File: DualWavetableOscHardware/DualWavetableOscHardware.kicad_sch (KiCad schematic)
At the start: 102 parts, among them J103 SWD Header, J106 CV1, J106 CV2, J106 MOD1, J106 MOD2, J106 OUT1, J106 OUT2, J109 Micro_SD_Card, J109 POWER, SW101 BOOT, SW101 RST, SW219 CH, SW219 MODE, SW221 ENC1, SW221 ENC2, U101 STM32F410CBTx, U106 AMS1117, U402 TL072, U403 PCM5100A, Y101 16MHz

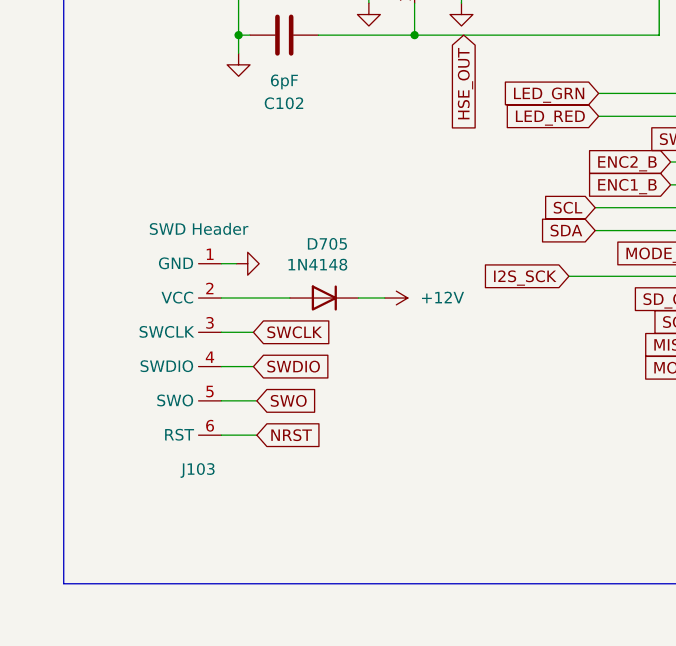
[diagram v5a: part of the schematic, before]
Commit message: new stackup/routing
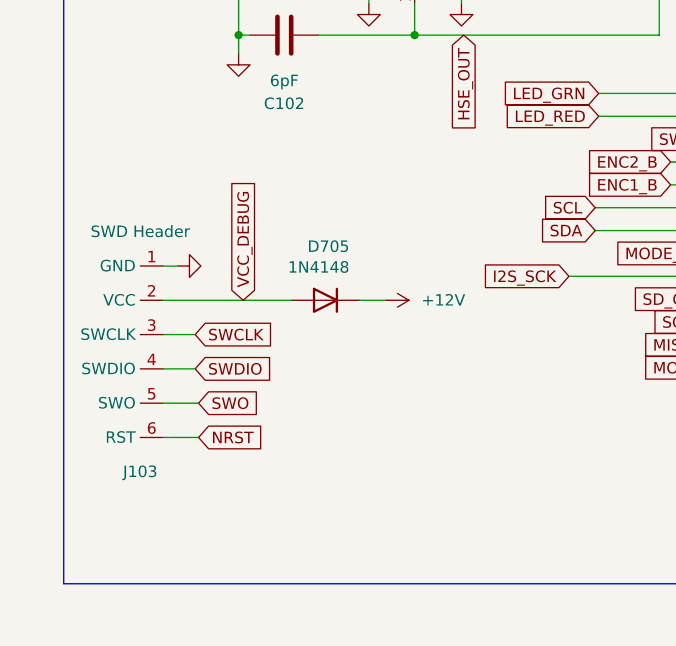
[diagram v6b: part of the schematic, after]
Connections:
- net VCC_DEBUG: now reaches D705.2 (A), J103.2 (VCC)
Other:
- moved on the sheet: J103
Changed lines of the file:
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@@
     (stroke (width 0) (type default))
   )
-  (wire (pts (xy 53.467 116.205) (xy 56.388 116.205))
+  (wire (pts (xy 53.594 116.459) (xy 56.515 116.459))
     (stroke (width 0) (type default))
   )
@@
     (stroke (width 0) (type default))
   )
-  (wire (pts (xy 38.227 116.205) (xy 45.847 116.205))
+  (wire (pts (xy 31.75 116.459) (xy 45.974 116.459))
     (stroke (width 0) (type default))
   )
@@
     (stroke (width 0) (type default))
   )
-  (wire (pts (xy 38.227 123.825) (xy 41.783 123.825))
+  (wire (pts (xy 31.75 124.079) (xy 35.306 124.079))
     (stroke (width 0) (type default))
   )
@@
     (stroke (width 0) (type default))
   )
-  (wire (pts (xy 38.227 120.015) (xy 41.783 120.015))
+  (wire (pts (xy 31.75 120.269) (xy 35.306 120.269))
     (stroke (width 0) (type default))
   )
@@
     (stroke (width 0) (type default))
   )
-  (wire (pts (xy 38.227 112.395) (xy 39.878 112.395))
+  (wire (pts (xy 31.75 112.649) (xy 33.401 112.649))
     (stroke (width 0) (type default))
   )
@@
     (stroke (width 0) (type default))
   )
-  (wire (pts (xy 38.227 131.445) (xy 42.164 131.445))
+  (wire (pts (xy 31.75 131.699) (xy 35.687 131.699))
     (stroke (width 0) (type default))
   )
@@
     (stroke (width 0) (type default))
   )
-  (wire (pts (xy 38.227 127.635) (xy 42.164 127.635))
+  (wire (pts (xy 31.75 127.889) (xy 35.687 127.889))
     (stroke (width 0) (type default))
   )
@@
     )
   )
-  (global_label "SWCLK" (shape input) (at 41.783 120.015 0) (fields_autoplaced)
+  (global_label "SWCLK" (shape input) (at 35.306 120.269 0) (fields_autoplaced)
     (effects (font (size 1.27 1.27)) (justify left))
-    (property "Intersheetrefs" "${INTERSHEET_REFS}" (at 50.9972 120.015 0)
+    (property "Intersheetrefs" "${INTERSHEET_REFS}" (at 44.5202 120.269 0)
       (effects (font (size 1.27 1.27)) (justify left) hide)
     )
@@
     )
   )
+  (global_label "VCC_DEBUG" (shape input) (at 40.64 116.459 90) (fields_autoplaced)
+    (effects (font (size 1.27 1.27)) (justify left))
+    (property "Intersheetrefs" "${INTERSHEET_REFS}" (at 40.64 102.5881 90)
+      (effects (font (size 1.27 1.27)) (justify left) hide)
+    )
+  )
   (global_label "SCL" (shape input) (at 79.756 106.172 180) (fields_autoplaced)
     (effects (font (size 1.27 1.27)) (justify right))
@@
     )
   )
-  (global_label "SWDIO" (shape input) (at 41.783 123.825 0) (fields_autoplaced)
+  (global_label "SWDIO" (shape input) (at 35.306 124.079 0) (fields_autoplaced)
     (effects (font (size 1.27 1.27)) (justify left))
-    (property "Intersheetrefs" "${INTERSHEET_REFS}" (at 50.6344 123.825 0)
+    (property "Intersheetrefs" "${INTERSHEET_REFS}" (at 44.1574 124.079 0)
       (effects (font (size 1.27 1.27)) (justify left) hide)
     )
@@
     )
   )
-  (global_label "NRST" (shape input) (at 42.164 131.445 0) (fields_autoplaced)
+  (global_label "NRST" (shape input) (at 35.687 131.699 0) (fields_autoplaced)
     (effects (font (size 1.27 1.27)) (justify left))
-    (property "Intersheetrefs" "${INTERSHEET_REFS}" (at 49.9268 131.445 0)
+    (property "Intersheetrefs" "${INTERSHEET_REFS}" (at 43.4498 131.699 0)
       (effects (font (size 1.27 1.27)) (justify left) hide)
     )
   )
-  (global_label "SWO" (shape input) (at 42.164 127.635 0) (fields_autoplaced)
+  (global_label "SWO" (shape input) (at 35.687 127.889 0) (fields_autoplaced)
     (effects (font (size 1.27 1.27)) (justify left))
-    (property "Intersheetrefs" "${INTERSHEET_REFS}" (at 49.1406 127.635 0)
+    (property "Intersheetrefs" "${INTERSHEET_REFS}" (at 42.6636 127.889 0)
       (effects (font (size 1.27 1.27)) (justify left) hide)
     )
@@
     )
   )
-  (symbol (lib_id "Diode:1N4148") (at 49.657 116.205 0) (mirror y) (unit 1)
+  (symbol (lib_id "Diode:1N4148") (at 49.784 116.459 0) (mirror y) (unit 1)
     (in_bom yes) (on_board yes) (dnp no)
-    (property "Reference" "D705" (at 52.324 110.236 0)
+    (property "Reference" "D705" (at 52.451 110.49 0)
       (effects (font (size 1.27 1.27)) (justify left))
     )
-    (property "Value" "1N4148" (at 52.324 112.5474 0)
+    (property "Value" "1N4148" (at 52.451 112.8014 0)
       (effects (font (size 1.27 1.27)) (justify left))
     )
-    (property "Footprint" "Diode_SMD:D_SOD-123" (at 49.657 116.205 0)
+    (property "Footprint" "Diode_SMD:D_SOD-123" (at 49.784 116.459 0)
       (effects (font (size 1.27 1.27)) hide)
     )
-    (property "Datasheet" "https://assets.nexperia.com/documents/data-sheet/1N4148_1N4448.pdf" (at 49.657 116.205 0)
+    (property "Datasheet" "https://assets.nexperia.com/documents/data-sheet/1N4148_1N4448.pdf" (at 49.784 116.459 0)
       (effects (font (size 1.27 1.27)) hide)
     )
-    (property "Sim.Device" "D" (at 49.657 116.205 0)
+    (property "Sim.Device" "D" (at 49.784 116.459 0)
       (effects (font (size 1.27 1.27)) hide)
     )
-    (property "Sim.Pins" "1=K 2=A" (at 49.657 116.205 0)
+    (property "Sim.Pins" "1=K 2=A" (at 49.784 116.459 0)
       (effects (font (size 1.27 1.27)) hide)
     )
@@
     )
   )
-  (symbol (lib_id "power:GND") (at 39.878 112.395 90) (unit 1)
+  (symbol (lib_id "power:GND") (at 33.401 112.649 90) (unit 1)
     (in_bom yes) (on_board yes) (dnp no) (fields_autoplaced)
-    (property "Reference" "#PWR0108" (at 46.228 112.395 0)
+    (property "Reference" "#PWR0108" (at 39.751 112.649 0)
       (effects (font (size 1.27 1.27)) hide)
     )
-    (property "Value" "GND" (at 43.688 112.395 0)
+    (property "Value" "GND" (at 37.211 112.649 0)
       (effects (font (size 1.27 1.27)) hide)
     )
-    (property "Footprint" "" (at 39.878 112.395 0)
+    (property "Footprint" "" (at 33.401 112.649 0)
       (effects (font (size 1.27 1.27)) hide)
     )
-    (property "Datasheet" "" (at 39.878 112.395 0)
+    (property "Datasheet" "" (at 33.401 112.649 0)
       (effects (font (size 1.27 1.27)) hide)
     )
@@
     )
   )
-  (symbol (lib_id "power:+12V") (at 56.388 116.205 270) (unit 1)
+  (symbol (lib_id "power:+12V") (at 56.515 116.459 270) (unit 1)
     (in_bom yes) (on_board yes) (dnp no) (fields_autoplaced)
-    (property "Reference" "#PWR0107" (at 52.578 116.205 0)
+    (property "Reference" "#PWR0107" (at 52.705 116.459 0)
       (effects (font (size 1.27 1.27)) hide)
     )
-    (property "Value" "+12V" (at 60.325 116.205 90)
+    (property "Value" "+12V" (at 60.452 116.459 90)
       (effects (font (size 1.27 1.27)) (justify left))
     )
-    (property "Footprint" "" (at 56.388 116.205 0)
+    (property "Footprint" "" (at 56.515 116.459 0)
       (effects (font (size 1.27 1.27)) hide)
     )
-    (property "Datasheet" "" (at 56.388 116.205 0)
+    (property "Datasheet" "" (at 56.515 116.459 0)
       (effects (font (size 1.27 1.27)) hide)
     )
@@
     )
   )
-  (symbol (lib_id "Connector:ST_SWDHeader_3Wire") (at 35.687 135.255 0) (unit 1)
+  (symbol (lib_id "Connector:ST_SWDHeader_3Wire") (at 29.21 135.509 0) (unit 1)
     (in_bom yes) (on_board yes) (dnp no) (fields_autoplaced)
-    (property "Reference" "J103" (at 35.687 135.255 0)
+    (property "Reference" "J103" (at 29.21 135.509 0)
       (effects (font (size 1.27 1.27)))
     )
-    (property "Value" "SWD Header" (at 35.687 108.585 0)
+    (property "Value" "SWD Header" (at 29.21 108.839 0)
       (effects (font (size 1.27 1.27)))
     )
-    (property "Footprint" "Connector_PinHeader_2.54mm:ST_SWHeader_3Wire_Pin" (at 35.687 126.365 0)
+    (property "Footprint" "Connector_PinHeader_2.54mm:ST_SWHeader_3Wire_Pin" (at 29.21 126.619 0)
       (effects (font (size 1.27 1.27)) hide)
     )
-    (property "Datasheet" "" (at 35.687 126.365 0)
+    (property "Datasheet" "" (at 29.21 126.619 0)
       (effects (font (size 1.27 1.27)) hide)
     )

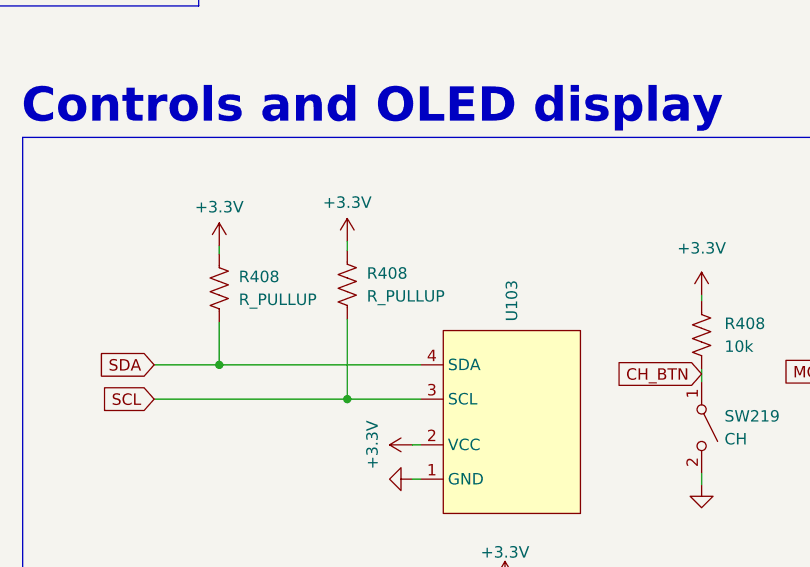
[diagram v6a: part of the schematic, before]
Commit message: wavetable voice logic
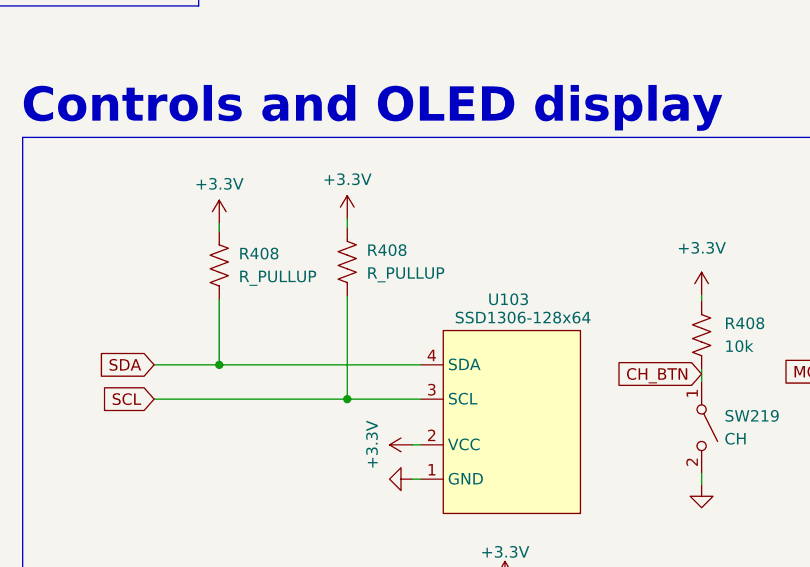
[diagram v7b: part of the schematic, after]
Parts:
- U103: value ~ -> SSD1306-128x64
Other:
- moved on the sheet: R408
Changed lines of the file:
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@@
     (stroke (width 0) (type default))
   )
-  (wire (pts (xy 211.963 182.753) (xy 211.963 191.643))
+  (wire (pts (xy 211.963 180.213) (xy 211.963 191.643))
     (stroke (width 0) (type default))
   )
@@
     (stroke (width 0) (type default))
   )
-  (wire (pts (xy 197.739 174.625) (xy 197.739 175.514))
+  (wire (pts (xy 197.739 172.085) (xy 197.739 172.974))
     (stroke (width 0) (type default))
   )
@@
     (stroke (width 0) (type default))
   )
-  (wire (pts (xy 211.963 174.117) (xy 211.963 175.133))
+  (wire (pts (xy 211.963 171.577) (xy 211.963 172.593))
     (stroke (width 0) (type default))
   )
@@
     (stroke (width 0) (type default))
   )
-  (wire (pts (xy 197.739 183.134) (xy 197.739 187.833))
+  (wire (pts (xy 197.739 180.594) (xy 197.739 187.833))
     (stroke (width 0) (type default))
   )
@@
     )
   )
-  (symbol (lib_id "power:+3.3V") (at 197.739 174.625 0) (unit 1)
+  (symbol (lib_id "power:+3.3V") (at 197.739 172.085 0) (unit 1)
     (in_bom yes) (on_board yes) (dnp no) (fields_autoplaced)
-    (property "Reference" "#PWR0136" (at 197.739 178.435 0)
+    (property "Reference" "#PWR0136" (at 197.739 175.895 0)
       (effects (font (size 1.27 1.27)) hide)
     )
-    (property "Value" "+3.3V" (at 197.739 170.307 0)
+    (property "Value" "+3.3V" (at 197.739 167.767 0)
       (effects (font (size 1.27 1.27)))
     )
-    (property "Footprint" "" (at 197.739 174.625 0)
+    (property "Footprint" "" (at 197.739 172.085 0)
       (effects (font (size 1.27 1.27)) hide)
     )
-    (property "Datasheet" "" (at 197.739 174.625 0)
+    (property "Datasheet" "" (at 197.739 172.085 0)
       (effects (font (size 1.27 1.27)) hide)
     )
@@
   )
   (symbol (lib_id "Display_Graphic:SSD1306_OLED_128x64") (at 235.331 194.183 270) (mirror x) (unit 1)
-    (in_bom yes) (on_board yes) (dnp no) (fields_autoplaced)
-    (property "Reference" "U103" (at 230.251 183.007 0)
+    (in_bom yes) (on_board yes) (dnp no)
+    (property "Reference" "U103" (at 227.584 180.594 90)
       (effects (font (size 1.27 1.27)) (justify left))
     )
-    (property "Value" "~" (at 235.331 194.183 0)
-      (effects (font (size 1.27 1.27)))
+    (property "Value" "SSD1306-128x64" (at 223.901 182.626 90)
+      (effects (font (size 1.27 1.27)) (justify left))
     )
     (property "Footprint" "Display:SSD1306_OLED_128x64" (at 240.411 194.183 0)
@@
     )
   )
-  (symbol (lib_id "power:+3.3V") (at 211.963 174.117 0) (unit 1)
+  (symbol (lib_id "power:+3.3V") (at 211.963 171.577 0) (unit 1)
     (in_bom yes) (on_board yes) (dnp no) (fields_autoplaced)
-    (property "Reference" "#PWR0139" (at 211.963 177.927 0)
+    (property "Reference" "#PWR0139" (at 211.963 175.387 0)
       (effects (font (size 1.27 1.27)) hide)
     )
-    (property "Value" "+3.3V" (at 211.963 169.799 0)
+    (property "Value" "+3.3V" (at 211.963 167.259 0)
       (effects (font (size 1.27 1.27)))
     )
-    (property "Footprint" "" (at 211.963 174.117 0)
+    (property "Footprint" "" (at 211.963 171.577 0)
       (effects (font (size 1.27 1.27)) hide)
     )
-    (property "Datasheet" "" (at 211.963 174.117 0)
+    (property "Datasheet" "" (at 211.963 171.577 0)
       (effects (font (size 1.27 1.27)) hide)
     )
@@
     )
   )
-  (symbol (lib_id "Device:R_US") (at 197.739 179.324 180) (unit 1)
+  (symbol (lib_id "Device:R_US") (at 197.739 176.784 180) (unit 1)
     (in_bom yes) (on_board yes) (dnp no) (fields_autoplaced)
-    (property "Reference" "R408" (at 199.898 178.054 0)
+    (property "Reference" "R408" (at 199.898 175.514 0)
       (effects (font (size 1.27 1.27)) (justify right))
     )
-    (property "Value" "R_PULLUP" (at 199.898 180.594 0)
+    (property "Value" "R_PULLUP" (at 199.898 178.054 0)
       (effects (font (size 1.27 1.27)) (justify right))
     )
-    (property "Footprint" "PCM_Resistor_SMD_AKL:R_0805_2012Metric" (at 196.723 179.07 90)
+    (property "Footprint" "PCM_Resistor_SMD_AKL:R_0805_2012Metric" (at 196.723 176.53 90)
       (effects (font (size 1.27 1.27)) hide)
     )
-    (property "Datasheet" "~" (at 197.739 179.324 0)
+    (property "Datasheet" "~" (at 197.739 176.784 0)
       (effects (font (size 1.27 1.27)) hide)
     )
@@
     )
   )
-  (symbol (lib_id "Device:R_US") (at 211.963 178.943 180) (unit 1)
+  (symbol (lib_id "Device:R_US") (at 211.963 176.403 180) (unit 1)
     (in_bom yes) (on_board yes) (dnp no) (fields_autoplaced)
-    (property "Reference" "R408" (at 214.122 177.673 0)
+    (property "Reference" "R408" (at 214.122 175.133 0)
       (effects (font (size 1.27 1.27)) (justify right))
     )
-    (property "Value" "R_PULLUP" (at 214.122 180.213 0)
+    (property "Value" "R_PULLUP" (at 214.122 177.673 0)
       (effects (font (size 1.27 1.27)) (justify right))
     )
-    (property "Footprint" "PCM_Resistor_SMD_AKL:R_0805_2012Metric" (at 210.947 178.689 90)
+    (property "Footprint" "PCM_Resistor_SMD_AKL:R_0805_2012Metric" (at 210.947 176.149 90)
       (effects (font (size 1.27 1.27)) hide)
     )
-    (property "Datasheet" "~" (at 211.963 178.943 0)
+    (property "Datasheet" "~" (at 211.963 176.403 0)
       (effects (font (size 1.27 1.27)) hide)
     )
